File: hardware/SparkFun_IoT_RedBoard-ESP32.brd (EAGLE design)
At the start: 68.6 x 58.4 mm, 230 parts, among them J1 5.5x2.1mm Barrel, J13 QWIIC_RIGHT_ANGLE, J15 MICRO-SD-PUSH-PUSH-EXT-PIN, J2 USB-C, J3 USB_SOLDER_PADS, J5 M10NO_SILK, Q1 MBT3904DW1T1, Q11 20V/4.2A/52mΩ/1.4W, Q13 20V/4.2A/52mΩ/1.4W, Q3 20V/4.2A/52mΩ/1.4W, Q5 20V/4.2A/52mΩ/1.4W, Q7 20V/4.2A/52mΩ/1.4W, Q9 20V/4.2A/52mΩ/1.4W, U1 ESP-WROOM-3232D, U2 CH340C, U3 LM1117, U4 3.3V, U5 MCP73831, U6 MAX17048

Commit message: Design Review Updates
Change "Revised by" to vector font in tDocu
Rename jumpers based on their functions
Add GND trace between GPIO 16/17 in layer 3
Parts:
- renumbered JP10 to MEAS, JP11 to I2C, JP12 to !ALERT!, JP13 to TCK, JP14 to TMS, JP15 to SHLD, JP16 to SD_DET, JP17 to LED_CHG, JP18 to LED_PWR, JP19 to LED_RX, JP20 to LED_TX, JP21 to LED_18
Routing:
- net GND: track 45.1 -> 73.1 mm, vias 153 -> 154

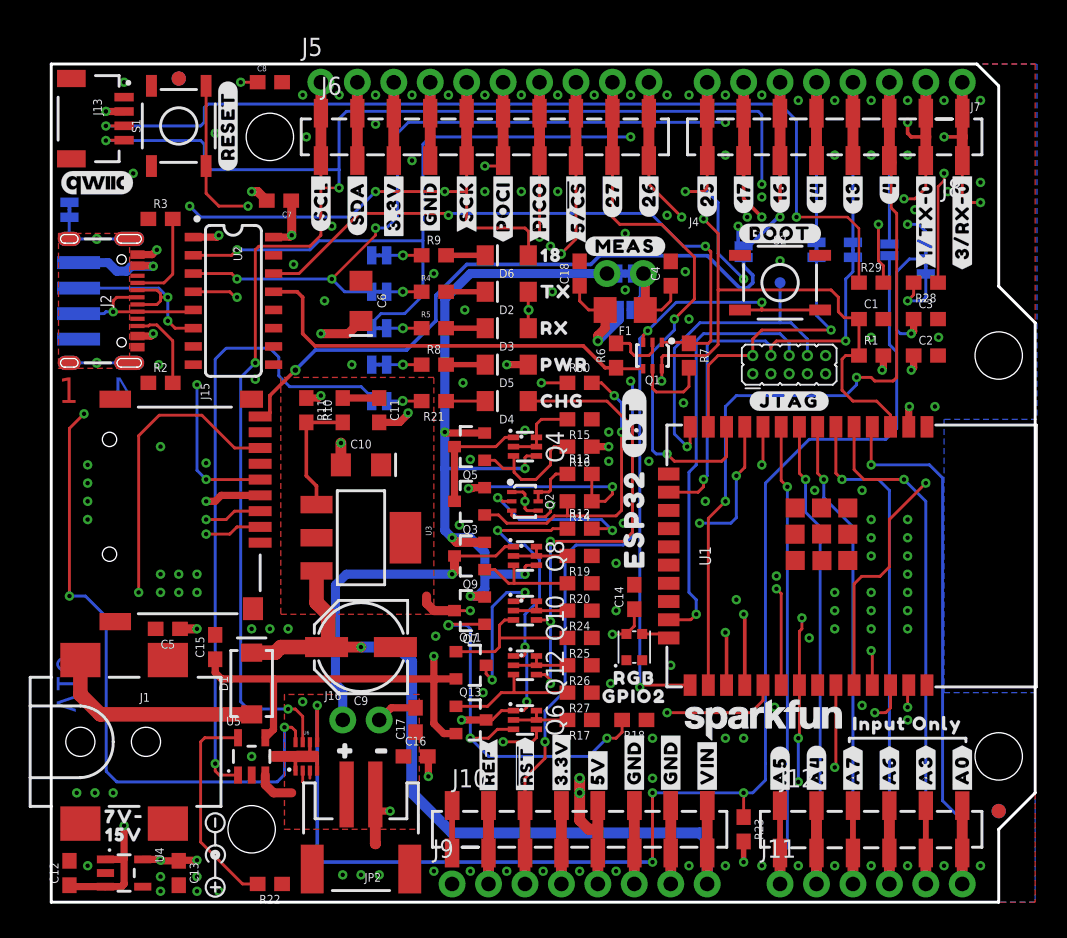
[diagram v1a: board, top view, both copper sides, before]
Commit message: Design review updates
Clean up SHLD jumper in schematic
Clean up boot mode table
Doot
Move C8 closer to CH340
Fix natural bridges
Improve GND continuity
Add 10uF cap to uSD
Switch 3V regulator
Replace LED footprints with non-hidden silk
Add NO jumper between RGB LED DO and NC pin
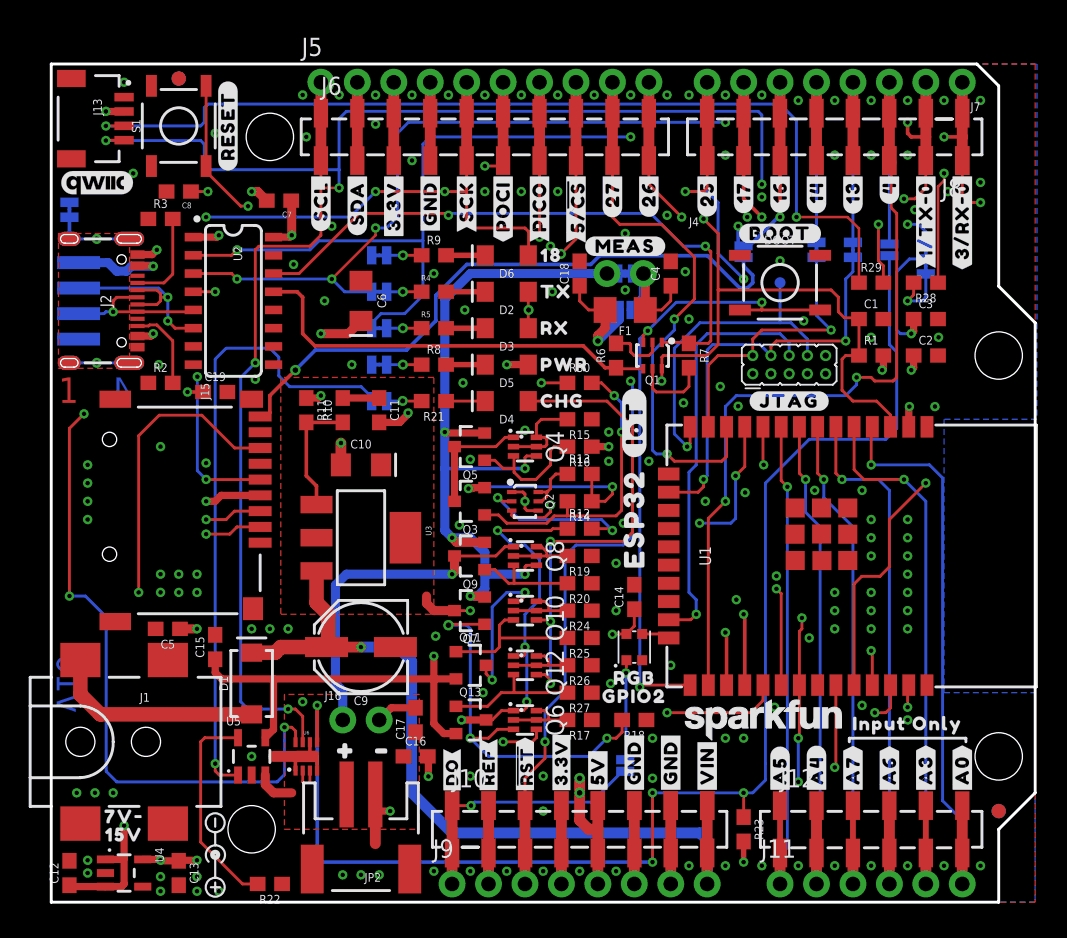
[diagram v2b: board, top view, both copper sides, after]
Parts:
- added C19: 10uF, SparkFun-Capacitors:0603
- added JP10: LED_DO, SparkFun-Jumpers:SMT-JUMPER_2_NO_SILK
- added U$114: (no value), output:#LED_DO#1
- added U$89: (no value), output:#DO#0
- added U$95: (no value), output:#LED_DO#0
- D2, D6: device SparkFun-LED:LED-1206-HIDDENSILK -> SparkFun-LED:LED-1206
- D3, D4: value YELLOW -> Yellow; device SparkFun-LED:LED-1206-HIDDENSILK -> SparkFun-LED:LED-1206
- D5: value GREEN -> RED; device SparkFun-LED:LED-1206-HIDDENSILK -> SparkFun-LED:LED-1206
- U4: value 3.3V -> XC6222B331MR-G
- moved C8 9.92 mm to (8.89, 49.5), turned to 180 degrees
- renumbered S2 to DOOT
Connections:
- new net LED_DO: J10.1, J9.1, JP10.2
- new net N$35: D7.DO, JP10.1
- net 3.3V: now also C19.1
- net GND: now also C19.2
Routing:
- net LED_DO: track 0.00 -> 18.5 mm, vias 0 -> 1
- net GND: track 73.1 -> 55.7 mm, vias 154 -> 162
- net N$6: track 20.4 -> 10.6 mm
- net N$35: track 0.00 -> 6.97 mm, vias 0 -> 1
- net ESP32_GPIO18_SCK: track 116.8 -> 114.9 mm
- net ESP32_GPIO19_POCI: track 150.4 -> 149.0 mm
- net N$12: track 5.46 -> 6.75 mm
- net 3.3V: track 49.9 -> 50.9 mm, vias 13 -> 14
- net ESP32_EN: track 122.6 -> 121.7 mm
- net ESP32_GPIO13_TCK: track 30.0 -> 29.2 mm
- net N$26: track 4.41 -> 5.10 mm
- net N$8: track 4.41 -> 5.10 mm
- net N$29: track 4.41 -> 5.10 mm
- net ESP32_SDA: track 193.2 -> 192.6 mm
- net ESP32_GPIO16: track 47.9 -> 48.5 mm
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- added copper zone on layer 15, net GND

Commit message: Pre-production updates
Update regulator current in schematic
Change "LED DO" silk label to "NC/LED DO"
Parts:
- removed U$95: (no value), output:#LED_DO#0
- added U$115: (no value), output:#NC#LED_DO#0
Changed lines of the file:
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@@
 <setting verticaltext="up"/>
 </settings>
-<grid distance="0.05" unitdist="inch" unit="inch" style="lines" multiple="1" display="yes" altdistance="0.004" altunitdist="inch" altunit="inch"/>
+<grid distance="0.05" unitdist="inch" unit="inch" style="lines" multiple="1" display="yes" altdistance="0.005" altunitdist="inch" altunit="inch"/>
 <layers>
 <layer number="1" name="Top" color="4" fill="1" visible="yes" active="yes"/>
@@
 </element>
 <element name="U$89" library="output" package="#DO#0" value="" x="27.94" y="7.493" smashed="yes" rot="R90"/>
-<element name="U$95" library="output" package="#LED_DO#0" value="" x="27.94" y="1.778" smashed="yes" rot="MR90"/>
 <element name="U$114" library="output" package="#LED_DO#1" value="" x="40.7416" y="9.5504" smashed="yes" rot="MR0"/>
+<element name="U$115" library="output" package="#NC#LED_DO#0" value="" x="27.94" y="1.778" smashed="yes" rot="MR90"/>
 </elements>
 <signals>
